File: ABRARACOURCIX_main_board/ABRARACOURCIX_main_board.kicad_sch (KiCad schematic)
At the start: 17 parts, among them U1 STM32F429VITx

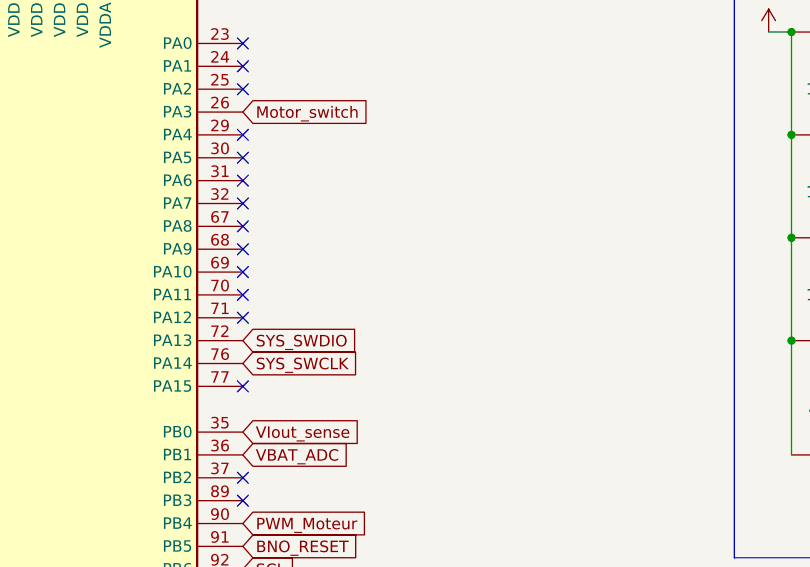
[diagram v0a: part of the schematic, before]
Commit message: micro_USB
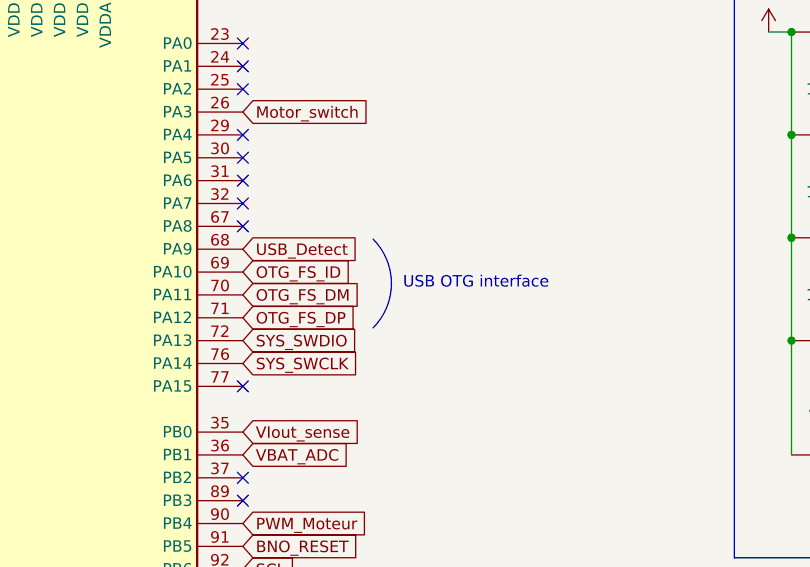
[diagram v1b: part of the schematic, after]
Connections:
- net USB_Detect: now reaches U1.68 (PA9)
- net OTG_FS_ID: now reaches U1.69 (PA10)
- net OTG_FS_DM: now reaches U1.70 (PA11)
- net OTG_FS_DP: now reaches U1.71 (PA12)
- no-connect marks 65 -> 61
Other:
- note added: "USB OTG interface"
